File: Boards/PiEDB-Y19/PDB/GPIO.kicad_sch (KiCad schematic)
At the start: 17 parts, among them SW2 SW_SPDT, SW3 SW_MEC_5E, U3 PCF8574

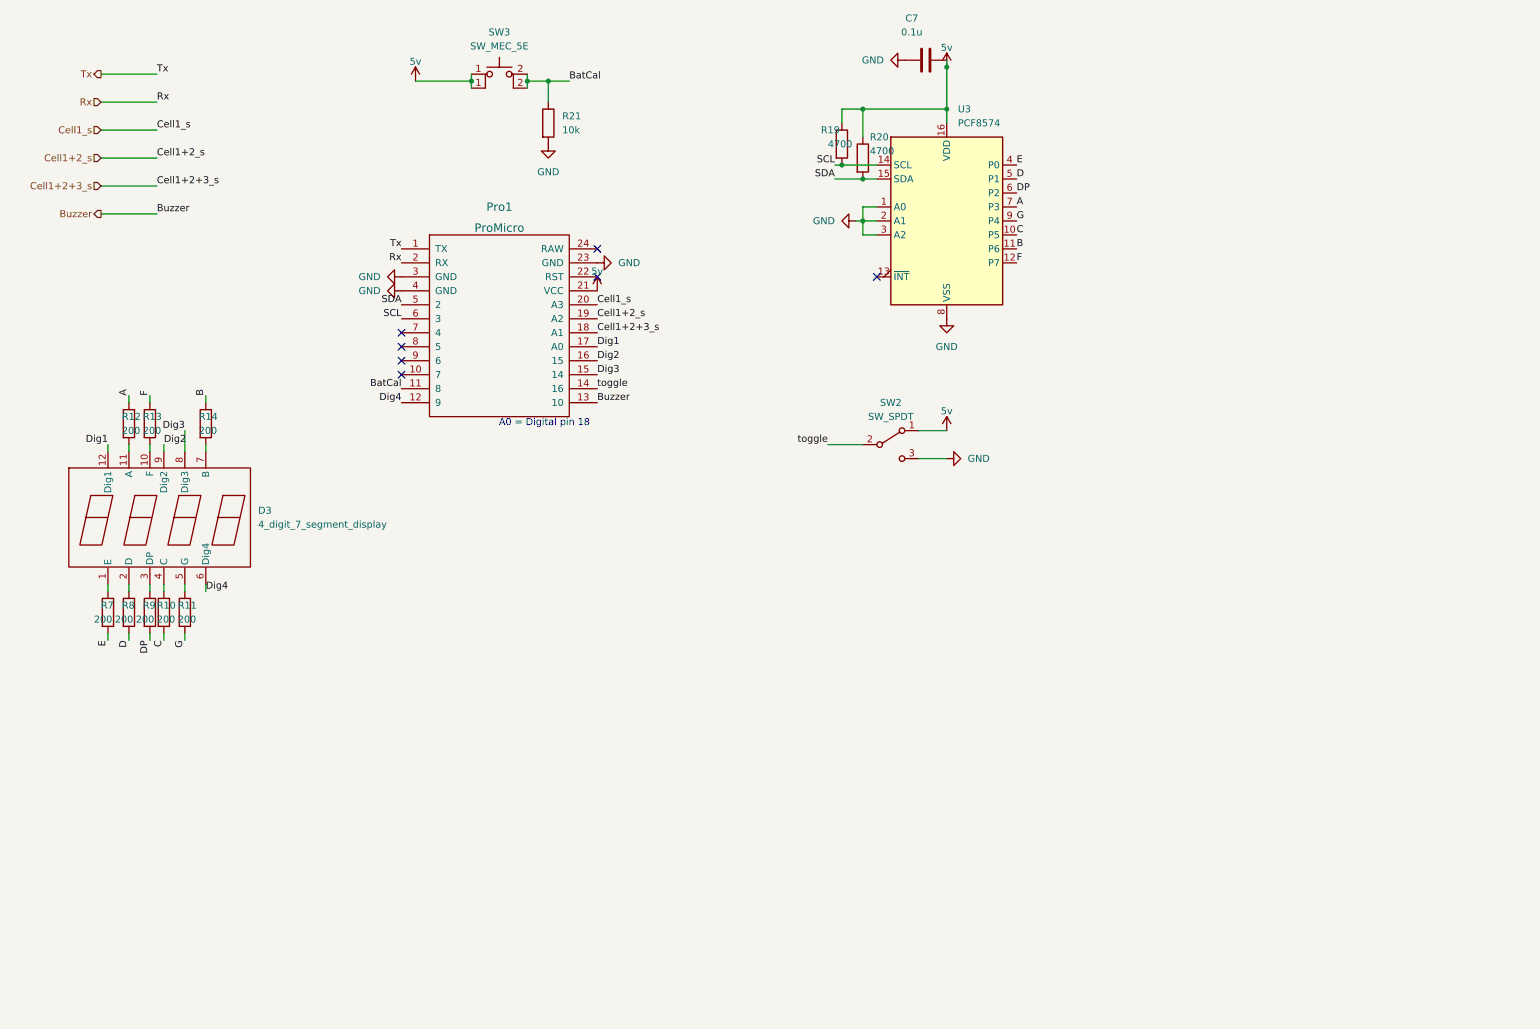
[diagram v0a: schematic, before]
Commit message: replaced pro micro and CH340G with ATMEGA32U4, added LM66100 power ORing, status LEDs, digit PNP drivers, and USB ESD; INITIAL LAYOUT
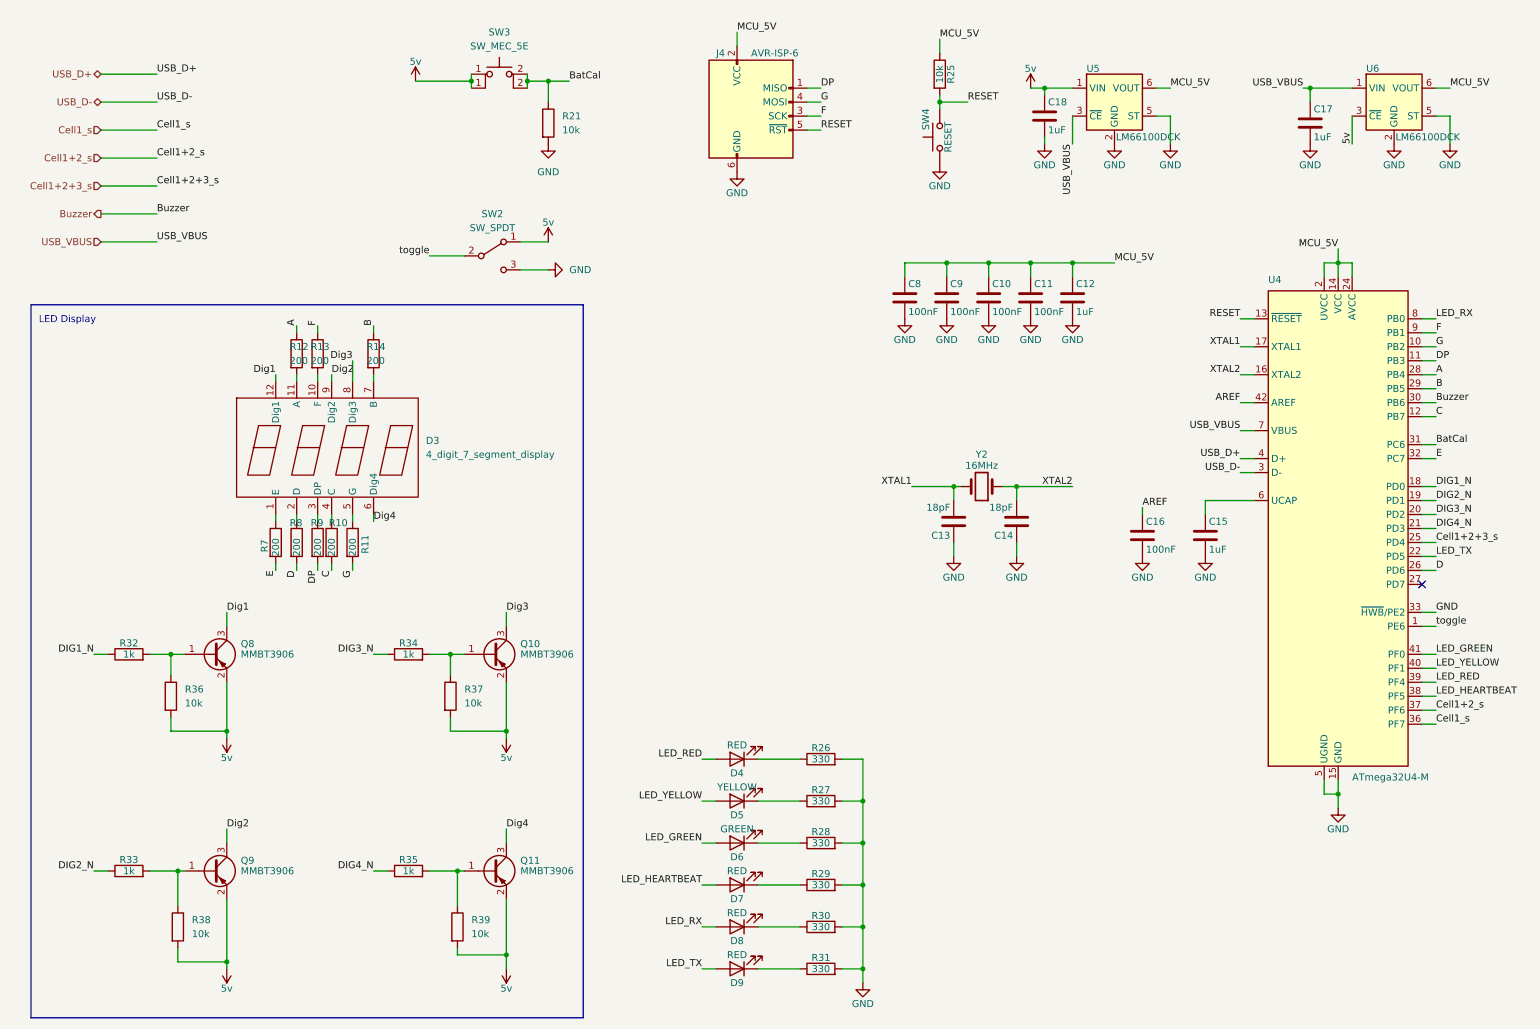
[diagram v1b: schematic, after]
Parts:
- removed C7: 0.1u, Capacitor_SMD:C_0603_1608Metric, symbol Device:C
- removed Pro1: ProMicro, PiE_Footprints:ProMicro-EnforcedTop, symbol PiE_Symbols:ProMicro
- removed R19, R20: 4700, Resistor_SMD:R_0603_1608Metric, symbol Device:R
- removed U3: PCF8574, PiE_Footprints:PCF8574T, symbol Interface_Expansion:PCF8574
- added C10, C11, C16, C8, C9: 100nF, Capacitor_SMD:C_0603_1608Metric, symbol Device:C
- added C12, C15, C17, C18: 1uF, Capacitor_SMD:C_0603_1608Metric, symbol Device:C
- added C13, C14: 18pF, Capacitor_SMD:C_0603_1608Metric, symbol Device:C
- added D4, D7, D8, D9: RED, LED_SMD:LED_0805_2012Metric, symbol Device:LED
- added D5: YELLOW, LED_SMD:LED_0805_2012Metric, symbol Device:LED
- added D6: GREEN, LED_SMD:LED_0805_2012Metric, symbol Device:LED
- added J4: AVR-ISP-6, Connector_PinHeader_2.54mm:PinHeader_2x03_P2.54mm_Vertical, symbol Connector:AVR-ISP-6
- added Q10, Q11, Q8, Q9: MMBT3906, Package_TO_SOT_SMD:SOT-23, symbol Transistor_BJT:MMBT3906
- added R25: 10k, Resistor_SMD:R_0603_1608Metric, symbol Device:R
- added R26, R27, R28, R29, R30, R31: 330, Resistor_SMD:R_0603_1608Metric, symbol Device:R
- added R32, R33, R34, R35: 1k, Resistor_SMD:R_0603_1608Metric, symbol Device:R
- added R36, R37, R38, R39: 10k, Resistor_SMD:R_0402_1005Metric, symbol Device:R
- added SW4: RESET, Button_Switch_THT:SW_PUSH_6mm, symbol Switch:SW_Push
- added U4: ATmega32U4-M, Package_DFN_QFN:QFN-44-1EP_7x7mm_P0.5mm_EP5.2x5.2mm, symbol MCU_Microchip_ATmega:ATmega32U4-M
- added U5, U6: LM66100DCK, Package_TO_SOT_SMD:SOT-363_SC-70-6, symbol Power_Management:LM66100DCK
- added Y2: 16MHz, Crystal:Crystal_SMD_5032-2Pin_5.0x3.2mm, symbol Device:Crystal
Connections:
- net 5v: now also C18.1, Q10.2 (E), Q11.2 (E), Q8.2 (E), Q9.2 (E), R36.2, R37.2, R38.2, R39.2, U5.1 (VIN), U6.3 (~{CE})
- net A: now also U4.28 (PB4)
- net B: now also U4.29 (PB5)
- net BatCal: now also U4.31 (PC6)
- net Buzzer: now also U4.30 (PB6)
- net C: now also U4.12 (PB7)
- net Cell1+2+3_s: now also U4.25 (PD4)
- net Cell1+2_s: now also U4.37 (PF6)
- net Cell1_s: now also U4.36 (PF7)
- net D: now also U4.26 (PD6)
- net DP: now also J4.1 (MISO), U4.11 (PB3)
- net Dig1: now also Q8.3 (C)
- net Dig2: now also Q9.3 (C)
- net Dig3: now also Q10.3 (C)
- net Dig4: now also Q11.3 (C)
- net E: now also U4.32 (PC7)
- net F: now also J4.3 (SCK), U4.9 (PB1)
- net G: now also J4.4 (MOSI), U4.10 (PB2)
- net GND: now also C10.2, C11.2, C12.2, C13.1, C14.1, C15.2, C16.2, C17.2, C18.2, C8.2, C9.2, J4.6 (GND), R26.2, R27.2, R28.2, R29.2, R30.2, R31.2, SW4.1, U4.15 (GND), U4.23 (GND), U4.33 (~{HWB}/PE2), U4.35 (GND), U4.43 (GND), U4.45 (GND), U4.5 (UGND), U5.2 (GND), U5.5 (ST), U6.2 (GND), U6.5 (ST)
- net toggle: now also U4.1 (PE6)
- new net: Q8.1 (B), R32.2, R36.1
- new net: D6.1 (K), R28.1
- new net: Q11.1 (B), R35.2, R39.1
- new net: D5.1 (K), R27.1
- new net: Q10.1 (B), R34.2, R37.1
- new net: D9.1 (K), R31.1
- new net: Q9.1 (B), R33.2, R38.1
- new net: D8.1 (K), R30.1
- new net: D7.1 (K), R29.1
- new net: C15.1, U4.6 (UCAP)
- new net: D4.1 (K), R26.1
- new net AREF: C16.1, U4.42 (AREF)
- new net DIG1_N: R32.1, U4.18 (PD0)
- new net DIG2_N: R33.1, U4.19 (PD1)
- new net DIG3_N: R34.1, U4.20 (PD2)
- new net DIG4_N: R35.1, U4.21 (PD3)
- new net LED_GREEN: D6.2 (A), U4.41 (PF0)
- new net LED_HEARTBEAT: D7.2 (A), U4.38 (PF5)
- new net LED_RED: D4.2 (A), U4.39 (PF4)
- new net LED_RX: D8.2 (A), U4.8 (PB0)
- new net LED_TX: D9.2 (A), U4.22 (PD5)
- new net LED_YELLOW: D5.2 (A), U4.40 (PF1)
- new net MCU_5V: C10.1, C11.1, C12.1, C8.1, C9.1, J4.2 (VCC), R25.1, U4.14 (VCC), U4.2 (UVCC), U4.24 (AVCC), U4.34 (VCC), U4.44 (AVCC), U5.6 (VOUT), U6.6 (VOUT)
- new net RESET: J4.5 (~{RST}), R25.2, SW4.2, U4.13 (~{RESET})
- new net USB_D+: U4.4 (D+)
- new net USB_D-: U4.3 (D-)
- new net USB_VBUS: C17.1, U4.7 (VBUS), U5.3 (~{CE}), U6.1 (VIN)
- new net XTAL1: C13.2, U4.17 (XTAL1), Y2.2
- new net XTAL2: C14.2, U4.16 (XTAL2), Y2.1
- no-connect marks 7 -> 1
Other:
- note added: "LED Display"
- note removed: "A0 = Digital pin 18"
- moved on the sheet: D3, R10, R11, R12, R13, R14, R7, R8, R9, SW2

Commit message: rerouted PDB to final satisfaction; need to add testpoints
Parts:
- added C19: 1uF, Capacitor_SMD:C_0603_1608Metric, symbol Device:C
- D4: Function LED_RED (PF4 / A3) -> BATT CRIT (PD0 / D3)
- D5: Function LED_YELLOW (PF1 / A4) -> BATT LOW (PD1 / D2)
- D6: Function LED_GREEN (PF0 / A5) -> BATT OK (PD2 / D0)
- D7: Function HEARTBEAT (PF5 / A2) -> HB (PD3 / D1)
- U4: footprint Package_DFN_QFN:QFN-44-1EP_7x7mm_P0.5mm_EP5.2x5.2mm -> PiE_Footprints:QFN-44-1EP_7x7mm_P0.5mm_EP5.2x5.2mm
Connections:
- net A: now also U4.36 (PF7); no longer U4.28 (PB4)
- net B: now also U4.38 (PF5); no longer U4.29 (PB5)
- net BatCal: now also J4.1 (MISO), U4.11 (PB3); no longer U4.31 (PC6)
- net Buzzer: now also J4.4 (MOSI), U4.10 (PB2); no longer U4.30 (PB6)
- net C: now also U4.39 (PF4); no longer U4.12 (PB7)
- net Cell1+2+3_s: now also U4.27 (PD7); no longer U4.25 (PD4)
- net Cell1+2_s: now also U4.26 (PD6); no longer U4.37 (PF6)
- net Cell1_s: now also U4.25 (PD4); no longer U4.36 (PF7)
- net D: now also U4.31 (PC6); no longer U4.26 (PD6)
- net DIG1_N: now also U4.29 (PB5); no longer U4.18 (PD0)
- net DIG2_N: now also U4.41 (PF0); no longer U4.19 (PD1)
- net DIG3_N: now also U4.1 (PE6); no longer U4.20 (PD2)
- net DIG4_N: now also U4.28 (PB4); no longer U4.21 (PD3)
- net DP: now also U4.32 (PC7); no longer J4.1 (MISO), U4.11 (PB3)
- net E: now also U4.30 (PB6); no longer U4.32 (PC7)
- net F: now also U4.37 (PF6); no longer J4.3 (SCK), U4.9 (PB1)
- net G: now also U4.40 (PF1); no longer J4.4 (MOSI), U4.10 (PB2)
- net GND: now also C19.2
- net LED_GREEN: now also U4.20 (PD2); no longer U4.41 (PF0)
- net LED_HEARTBEAT: now also U4.21 (PD3); no longer U4.38 (PF5)
- net LED_RED: now also U4.18 (PD0); no longer U4.39 (PF4)
- net LED_YELLOW: now also U4.19 (PD1); no longer U4.40 (PF1)
- net MCU_5V: now also C19.1
- net toggle: now also U4.12 (PB7); no longer U4.1 (PE6)
- new net ISP_SCK: J4.3 (SCK), U4.9 (PB1)
- no-connect marks 1 -> 0

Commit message: added test points to board and revA silkscreen, as well as general silkscreen text that will help board readability
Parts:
- added 5V1, GND1, MCU_5V1, USB_VBUS1: TestPoint, TestPoint:TestPoint_Loop_D2.60mm_Drill0.9mm_Beaded, symbol Connector:TestPoint
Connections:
- net 5v: now also 5V1.1
- net GND: now also GND1.1
- net MCU_5V: now also MCU_5V1.1
- net USB_VBUS: now also USB_VBUS1.1
